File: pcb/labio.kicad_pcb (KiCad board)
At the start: 2 copper layers, 152 x 85 mm, 235 parts, among them IC201 dnp-AT24CS32-XHM, J701 JACK_TRRS_6PINS, P201 CONN_02X20, P301 CONN_01X04, P302 CONN_01X04, P303 CONN_01X04, P401 SFV12R-1ST__HLF, P601 CONN_01X02, P602 CONN_01X02, P603 CONN_01X04, P604 CONN_01X02, P605 CONN_01X03, P606 CONN_01X03, P607 CONN_01X05, P608 CONN_01X05, P701 CONN_01X04, P702 CONN_01X04, P703 CONN_01X04, P704 CONN_01X02, P901 CONN_01X06, Q301 PHOTOTRANSISTOR, Q302 Q_NMOS_GSD, Q303 Q_NMOS_GSD, Q601 Q_NMOS_GSD, Q602 Q_NMOS_GSD, Q603 Q_NMOS_GSD, Q604 Q_NMOS_GSD, Q605 Q_NMOS_GSD, Q606 Q_NMOS_GSD, Q607 Q_NMOS_GSD, Q608 Q_NMOS_GSD, Q609 Q_NMOS_GSD, Q610 Q_NMOS_GSD, Q611 Q_NMOS_GSD, Q612 Q_NMOS_GSD, Q613 Q_NMOS_GSD, SW301 DIP_SWITCH_X04, SW401 DIP_SWITCH_X04, SW501 DIP_SWITCH_X04, SW601 DIP_SWITCH_X04, SW602 DIP_SWITCH_X04, SW603 DIP_SWITCH_X04, SW604 DIP_SWITCH_X04, SW605 ROT_ENC, SW606 DIP_SWITCH_X04, SW701 DIP_SWITCH_X04, SW702 DIP_SWITCH_X04, SW801 SW_PUSH, SW802 SW_PUSH, SW803 SW_PUSH, SW804 SW_PUSH, SW805 SW_PUSH, U201 AP7365_SOT-23-5, U301 ADS1015, U501 LSM303D, U502 BMP280, U503 L3GD20H, U601 L298P_PowerSO20, U701 SPU0410HR5H, U702 WM8750, U703 OPA344_SOT23-5

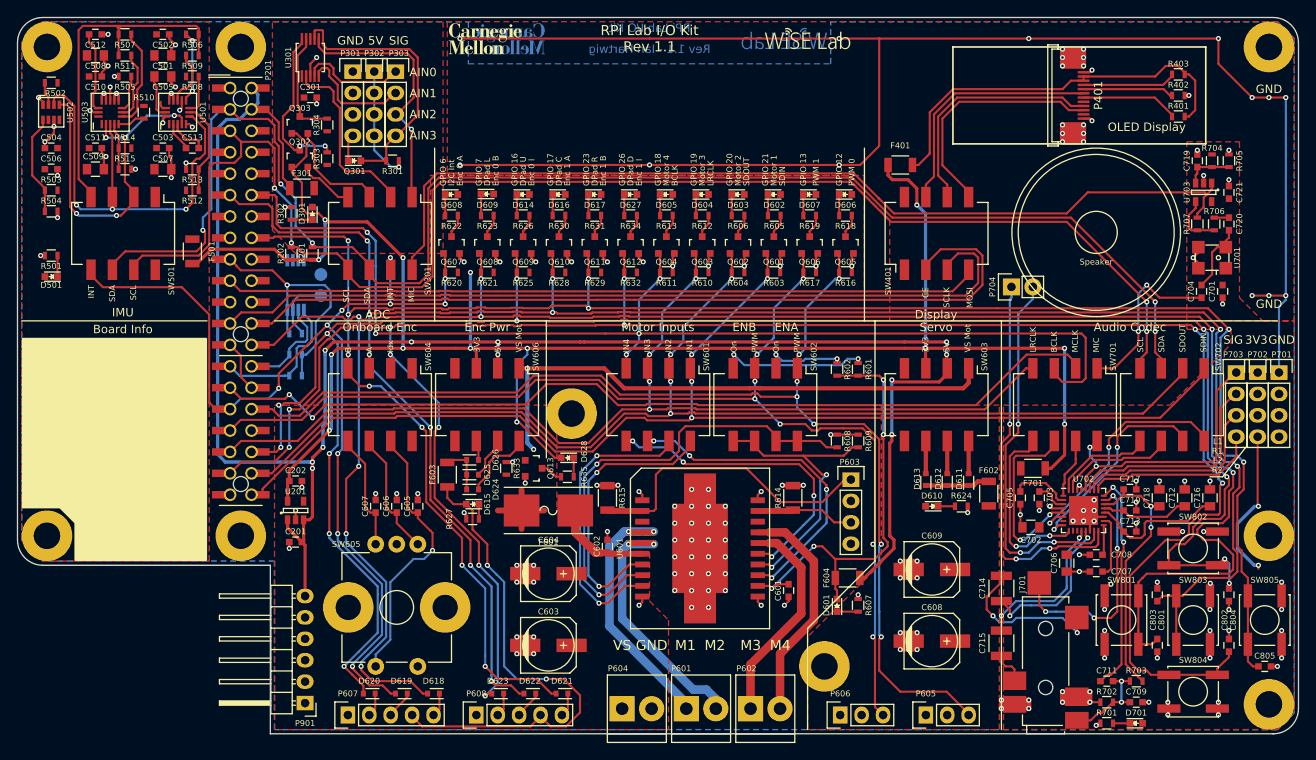
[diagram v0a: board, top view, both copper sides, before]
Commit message: Fix i2c addresses, pressure sensor footprint, consolidate BOM
* Schematic should list I2C addresses for accelerometer, gyro.
* Pressure sensor footprint (U502) has pins in the wrong order. Redraw footprint and adjust routing.
* Bump i2c and photodiode pullups to 2.2k
* Remove R505 near gyro
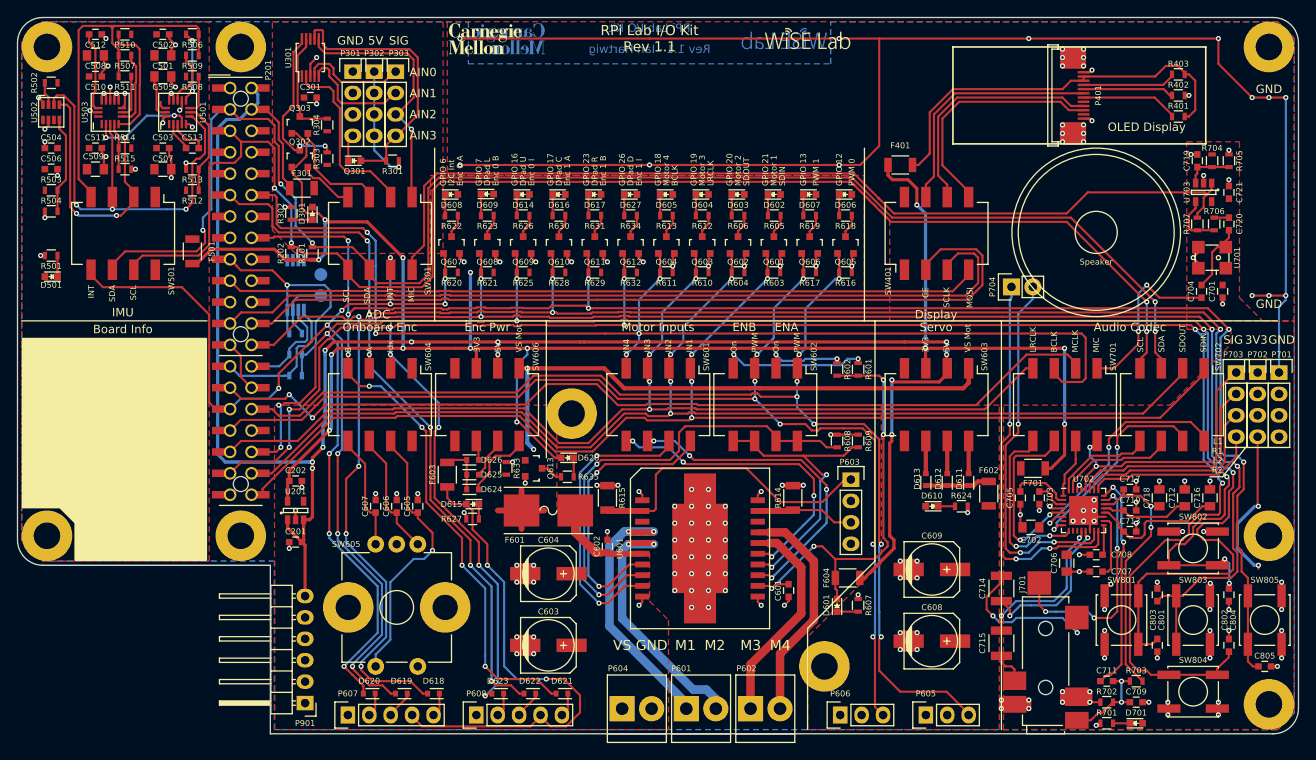
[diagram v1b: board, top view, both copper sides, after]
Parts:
- removed R505: 0, Resistors_SMD:R_0603
- R201, R202: value 4.7k -> 2.2k
- R301: value 1.5k -> 2.2k
- moved R510 9.52 mm to (89.8, 52.0), turned to 180 degrees
- moved R507 2.50 mm to (89.8, 54.5)
- moved R511 2.50 mm to (89.8, 57.0)
- turned R503 to 0 degrees
- turned R504 to 180 degrees
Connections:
- U503 pad 8: Net-(R505-Pad1) -> GND
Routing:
- net /labio-imu/GYRO_CS: track 3.27 -> 14.6 mm
- net Net-(R505-Pad1): track 4.41 -> 0.00 mm
- net /labio-imu/GYRO_INT1: track 8.27 -> 5.15 mm
- net /labio-imu/GYRO_INT2: track 11.9 -> 8.83 mm
- net /labio-imu/INT_J: track 42.2 -> 45.0 mm

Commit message: using MISO/gpio for D/C on led screen and layout. bump to rev 1.2.0.
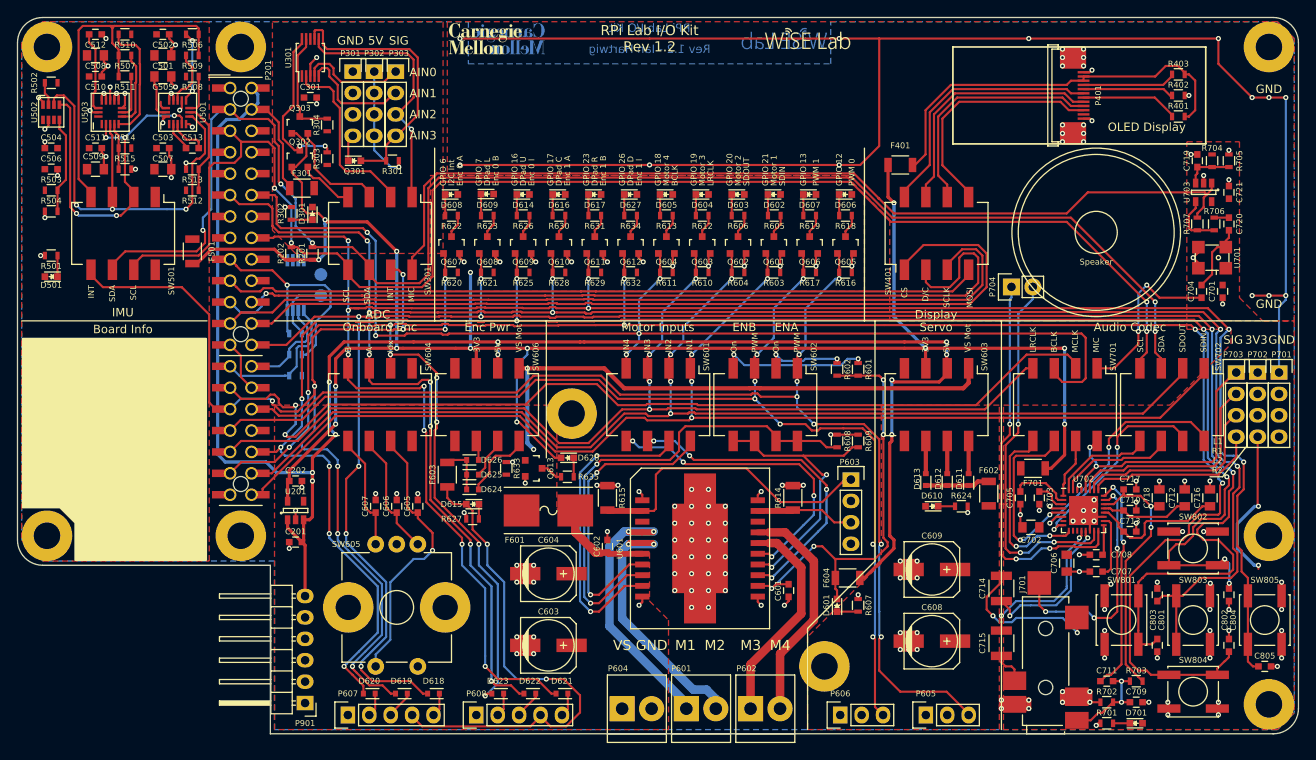
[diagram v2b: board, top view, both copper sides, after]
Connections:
- H1001 pad 1: (no net) -> Net-(H1001-Pad1)
- H1002 pad 1: (no net) -> Net-(H1002-Pad1)
- H1003 pad 1: (no net) -> Net-(H1003-Pad1)
- H1004 pad 1: (no net) -> Net-(H1004-Pad1)
- H1005 pad 1: (no net) -> Net-(H1005-Pad1)
- H1006 pad 1: (no net) -> Net-(H1006-Pad1)
- H1007 pad 1: (no net) -> Net-(H1007-Pad1)
- H1008 pad 1: (no net) -> Net-(H1008-Pad1)
- H1009 pad 1: (no net) -> Net-(H1009-Pad1)
- J701 pad 6: (no net) -> Net-(J701-Pad6)
- P201 pad 21: /labio-rpi/GPIO9_SPI0_MISO -> /labio-display/DC
- P401 pad 11: (no net) -> Net-(P401-Pad11)
- P401 pad 8: (no net) -> /labio-display/OLED_DC
- P901 pad 5: (no net) -> Net-(P901-Pad5)
- SW401 pad 1: (no net) -> /labio-rpi/GPIO8_SPI0_CE0_N
- SW401 pad 2: /labio-rpi/GPIO8_SPI0_CE0_N -> /labio-display/DC
- SW401 pad 7: /labio-display/~OLED_CS -> /labio-display/OLED_DC
- SW401 pad 8: (no net) -> /labio-display/~OLED_CS
- SW501 pad 1: (no net) -> Net-(SW501-Pad1)
- SW501 pad 8: (no net) -> Net-(SW501-Pad8)
- SW603 pad 4: (no net) -> Net-(SW603-Pad4)
- SW603 pad 5: (no net) -> Net-(SW603-Pad5)
- SW604 pad 1: (no net) -> Net-(SW604-Pad1)
- SW604 pad 8: (no net) -> Net-(SW604-Pad8)
- SW606 pad 4: (no net) -> Net-(SW606-Pad4)
- SW606 pad 5: (no net) -> Net-(SW606-Pad5)
- U702 pad 10: (no net) -> Net-(U702-Pad10)
- U702 pad 11: (no net) -> Net-(U702-Pad11)
- U702 pad 7: (no net) -> Net-(U702-Pad7)
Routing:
- net /labio-display/DC: track 0.00 -> 107.1 mm, vias 0 -> 1
- net /labio-display/OLED_DC: track 0.00 -> 29.4 mm
- net Net-(J701-Pad6): track 0.00 -> 12.2 mm, vias 0 -> 4
- net (no net): track 35.2 -> 23.0 mm, vias 16 -> 12
- net /labio-dio/VS_MOTOR: track 76.4 -> 66.3 mm
- net /labio-dpad/DPAD_UP: track 227.9 -> 218.8 mm, vias 12 -> 11
- net /GPCLK1: track 109.9 -> 116.1 mm
- net /labio-rpi/GPIO8_SPI0_CE0_N: track 100.8 -> 105.1 mm
- net /labio-dpad/DPAD_DOWN: track 252.5 -> 256.5 mm, vias 11 -> 12
- net /I2C_INT: track 126.2 -> 130.0 mm, vias 10 -> 9
- net /labio-dpad/DPAD_RIGHT: track 237.4 -> 241.0 mm
- net /labio-dpad/DPAD_CENTER: track 242.8 -> 245.7 mm, vias 10 -> 11
- net /labio-dio/MOT_ENA: track 56.0 -> 58.1 mm
- net /labio-dio/MOT_IN2_J: track 34.9 -> 36.9 mm
- net /labio-dio/MOT_IN1_J: track 33.7 -> 35.7 mm
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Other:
- board text added: "CS"
- board text added: "D/C"
- board text added: "RPi Lab I/O Kit Rev 1.2"
- board text added: "Rev 1.2 - Ian Hartwig"
- board text removed: "CE"
- board text removed: "RPi Lab I/O Kit Rev 1.1"
- board text removed: "Rev 1.1 - Ian Hartwig"

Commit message: add options for driving oled reset. no changes to stuffed bom parts.
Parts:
- added C401: 4.7uF, Capacitors_SMD:C_0805, F.Cu at (219.8, 63.0)
- added R404: dnp-0, Resistors_SMD:R_0603, F.Cu at (211.5, 59.2)
- added R405: 47k, Resistors_SMD:R_0603, F.Cu at (214.8, 61.8)
- added R406: dnp-0, Resistors_SMD:R_0603, F.Cu at (214.8, 59.2)
- moved R401 3.25 mm to (211.5, 61.8)
- moved R403 3.25 mm to (211.5, 56.8)
- moved R402 2.50 mm to (214.8, 56.8)
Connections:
- F401 pad 2: Net-(F401-Pad2) -> /labio-display/VDD_3V3_F
- P401 pad 2: Net-(F401-Pad2) -> /labio-display/VDD_3V3_F
- P401 pad 3: Net-(F401-Pad2) -> /labio-display/VDD_3V3_F
- R401 pad 1: /labio-display/~OLED_RES -> /labio-dpad/DPAD_UP
- R401 pad 2: Net-(F401-Pad2) -> /labio-display/~OLED_RES
- R403 pad 2: Net-(F401-Pad2) -> /labio-display/VDD_3V3_F
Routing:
- net /labio-display/VDD_3V3_F: track 0.00 -> 49.4 mm
- net Net-(F401-Pad2): track 47.7 -> 0.00 mm
- net /labio-dpad/DPAD_UP: track 218.8 -> 257.4 mm, vias 11 -> 12
- net /labio-rpi/GPIO8_SPI0_CE0_N: track 105.1 -> 133.9 mm, vias 0 -> 2
- net /labio-display/~OLED_CS: track 30.9 -> 42.3 mm
- net /labio-display/~OLED_RES: track 11.5 -> 19.6 mm
- net /labio-display/OLED_BS0: track 11.1 -> 7.77 mm
- net GND: track 412.8 -> 414.3 mm, vias 181 -> 183
